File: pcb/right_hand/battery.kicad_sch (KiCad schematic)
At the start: 43 parts

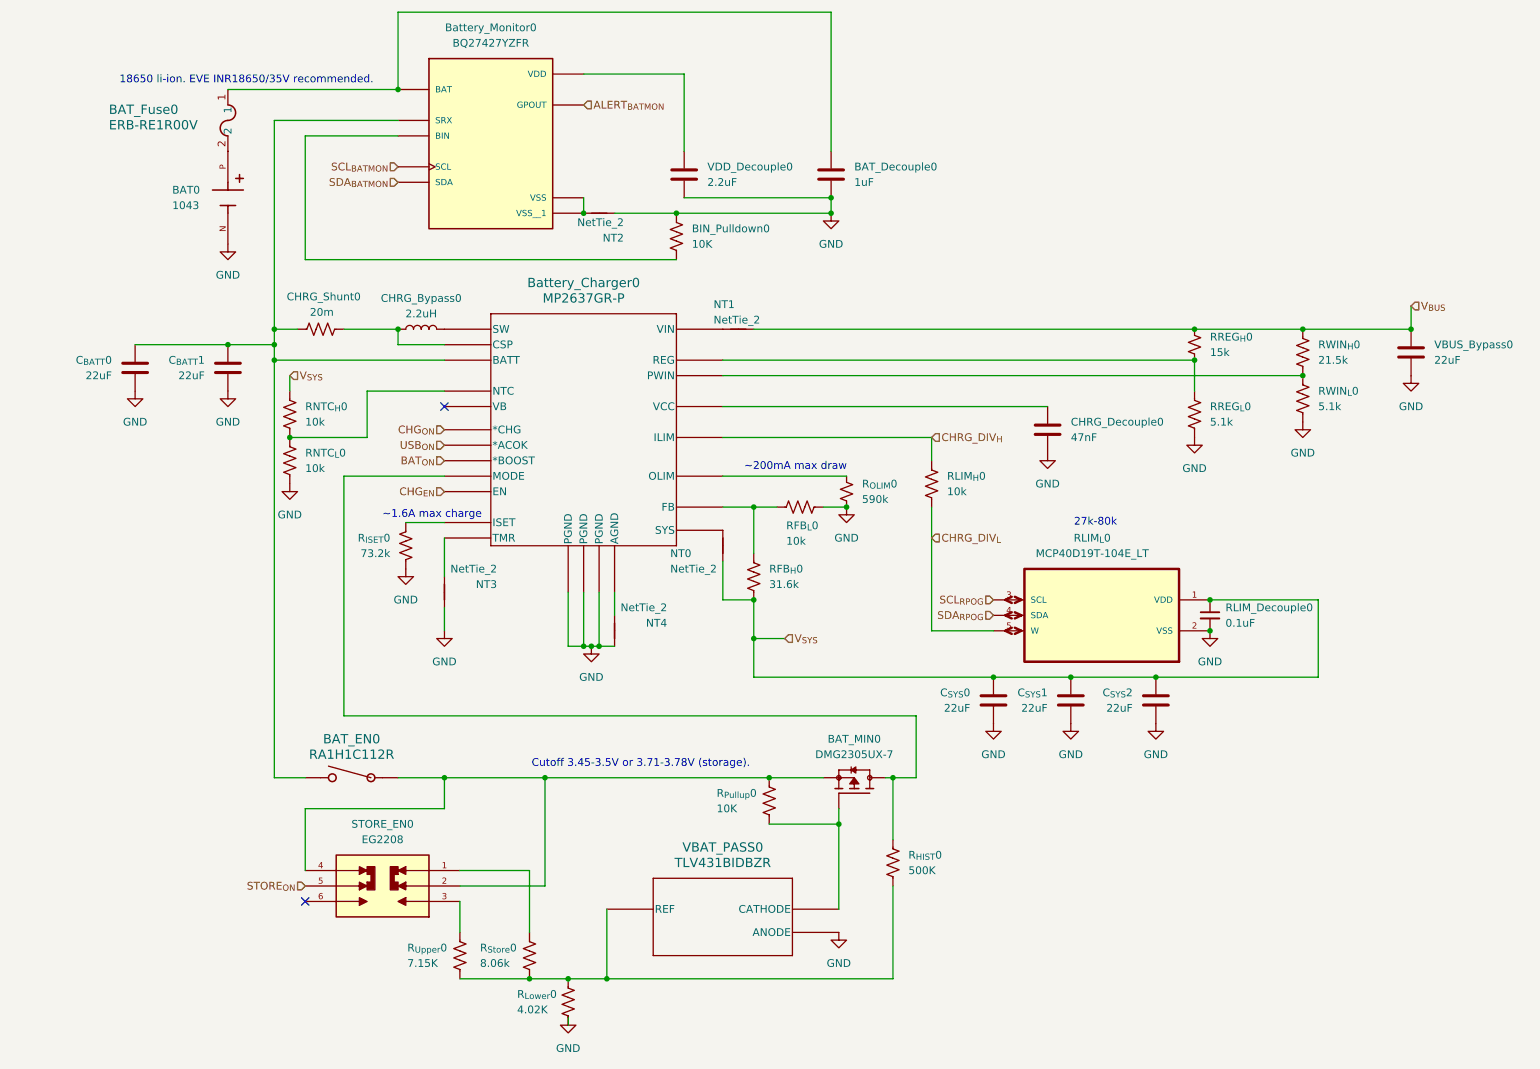
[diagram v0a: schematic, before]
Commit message: Add more ESD protection
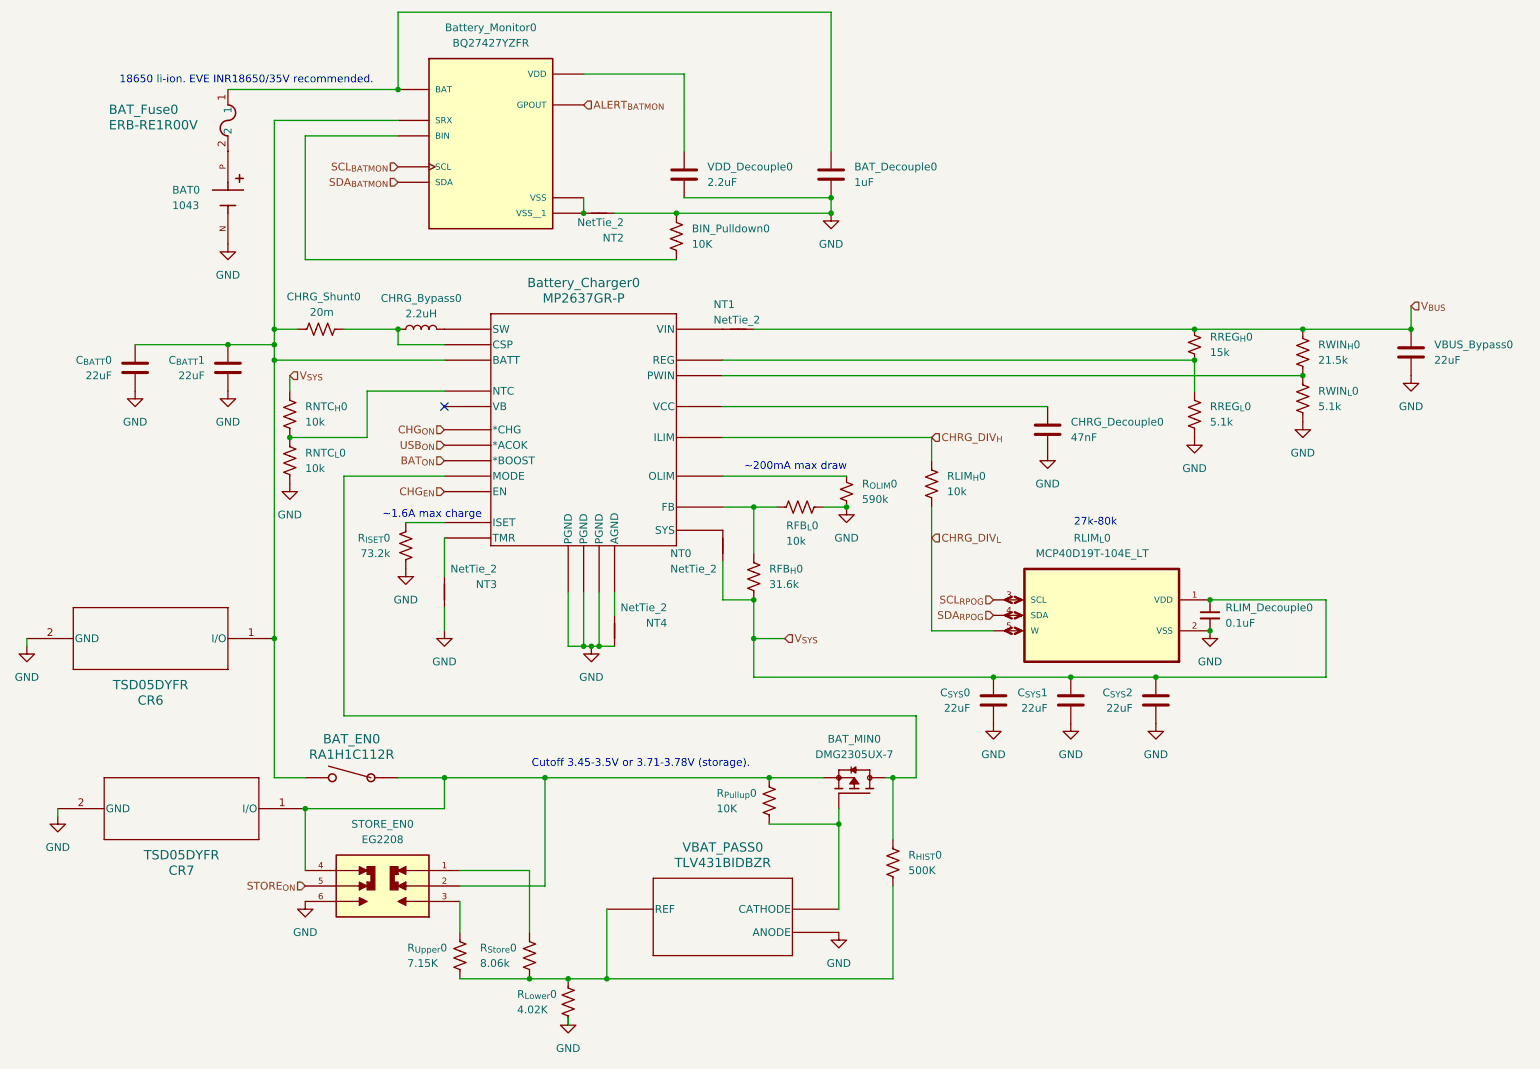
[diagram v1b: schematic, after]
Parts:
- added CR6, CR7: TSD05DYFR, TVS_SOD2_DYF_TEX, symbol TSD05DYFR:TSD05DYFR
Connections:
- net GND: now also STORE_EN0.6, CR6.2 (GND), CR7.2 (GND)
- net at BAT_EN0.1, BAT_MIN0.2, R_{Pullup}0.1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: now also CR7.1 (I/O)
- net at BAT_EN0.2, Battery_Charger0.5 (BATT), Battery_Monitor0.C2 (SRX)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: now also CR6.1 (I/O)
- no-connect marks 2 -> 1
